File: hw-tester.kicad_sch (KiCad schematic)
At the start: 50 parts, among them J1 AVR-ISP-6, J10 Conn_01x08, J11 Conn_01x08, J12 Conn_01x08, J13 Conn_01x08, J14 BarrelJack, J15 Conn_01x08, J16 Conn_01x08, J17 Conn_01x08, J18 Conn_01x08, J19 USB_B_Mini, J2 Conn_01x08, J3 Conn_01x08, J4 Conn_01x08, J5 Conn_01x08, J6 Conn_01x08, J7 Conn_01x08, J8 Conn_01x08, J9 Conn_01x08, U15 ATmega324PA-M, U28 FT230XQ, U30 ADuM1201AR, X1 IQXO-70

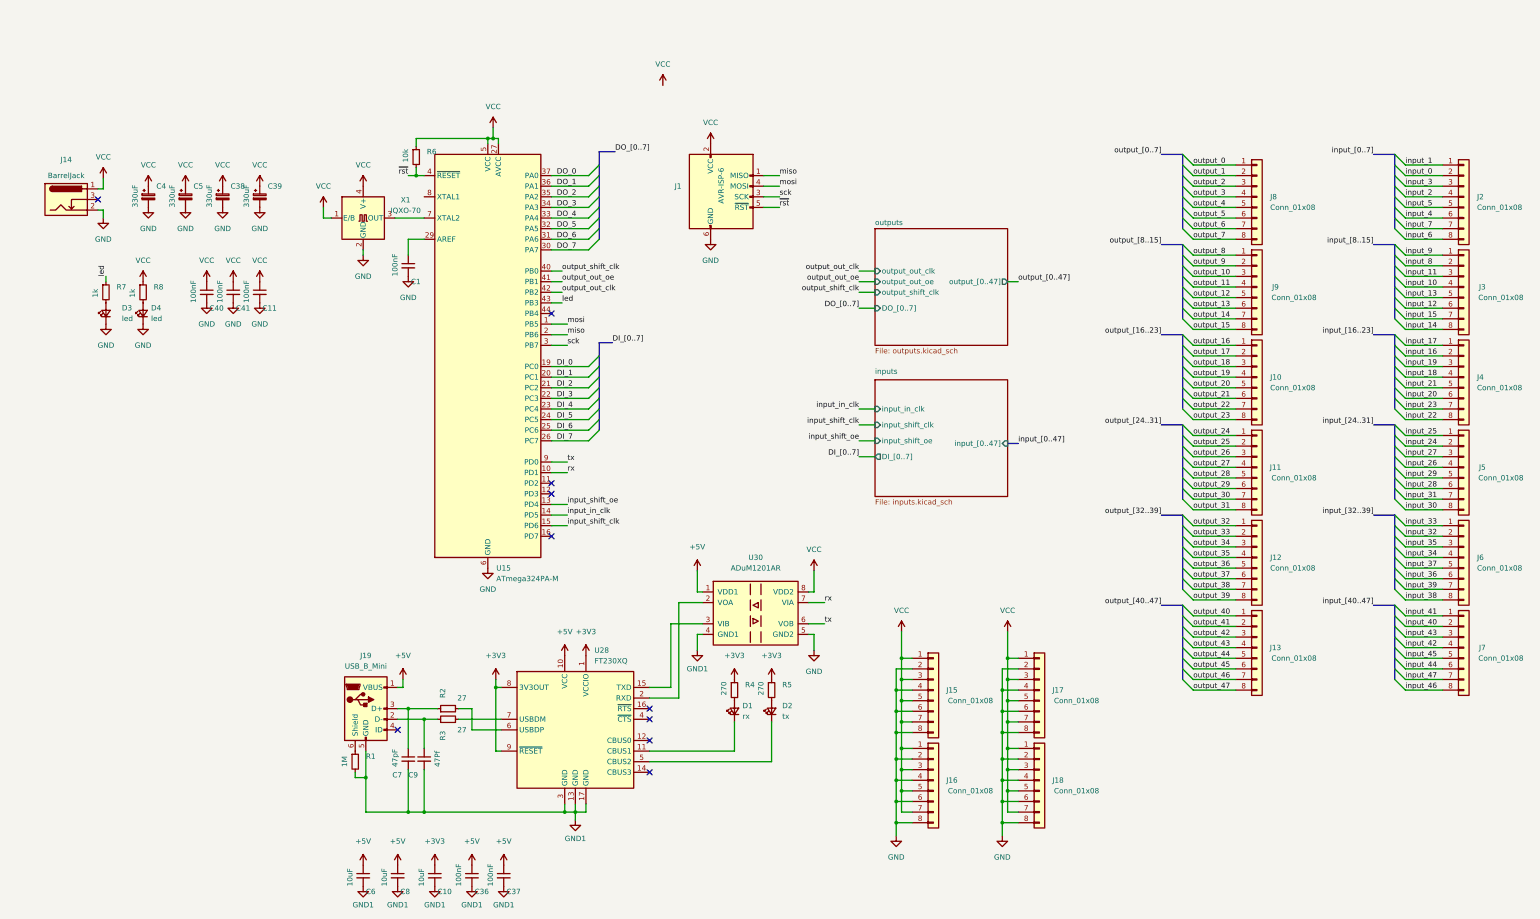
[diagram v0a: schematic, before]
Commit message: Turns out 324As don't really exist anymore
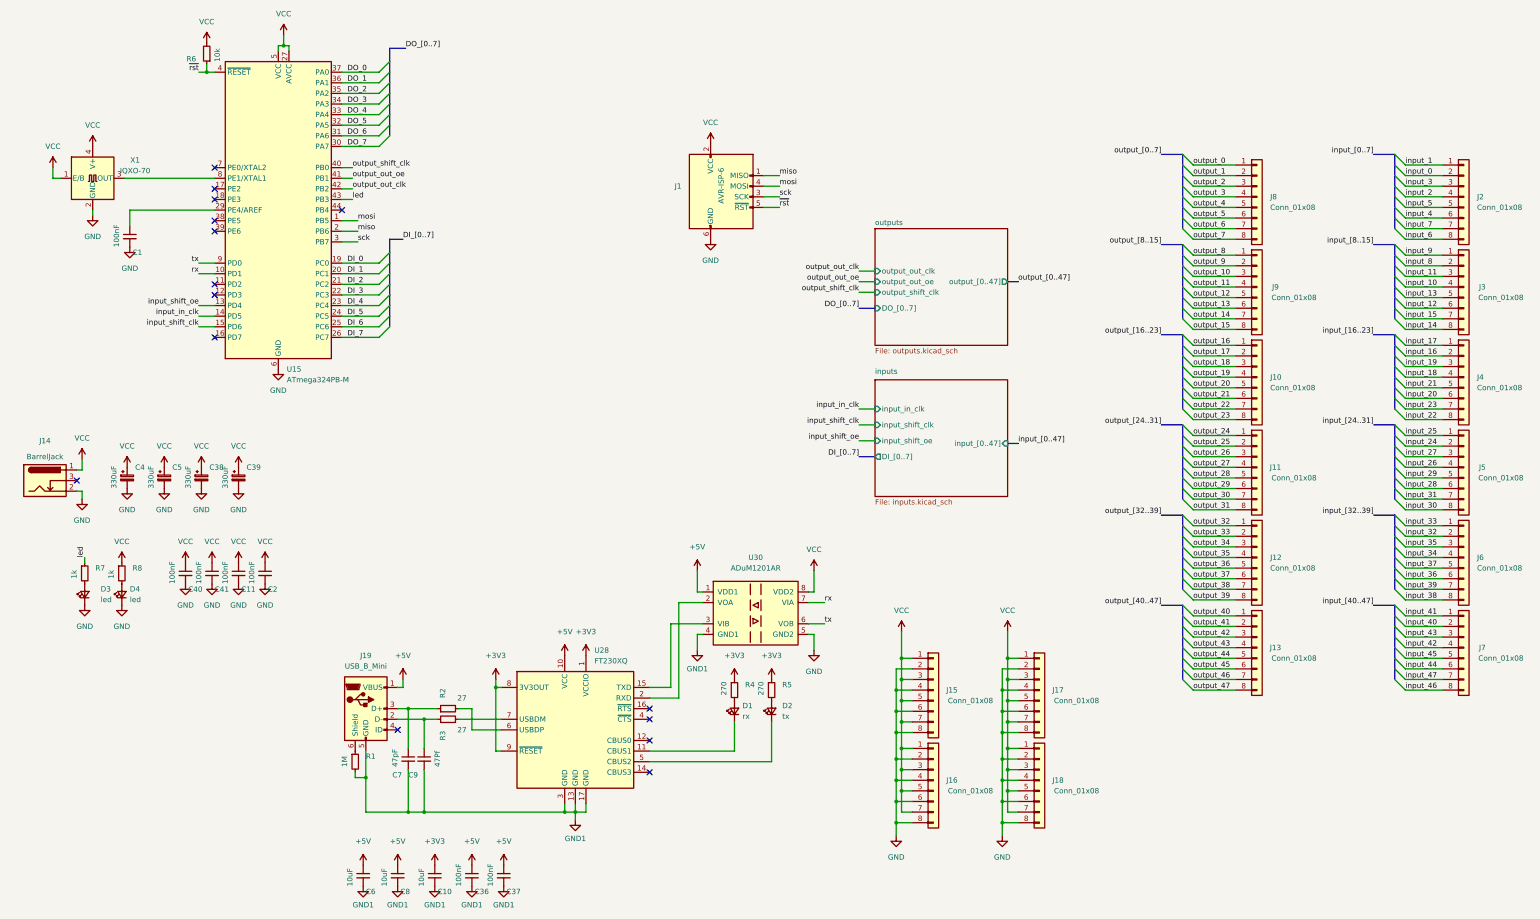
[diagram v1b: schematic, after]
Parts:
- removed U15: ATmega324PA-M, Package_DFN_QFN:QFN-44-1EP_7x7mm_P0.5mm_EP5.2x5.2mm, symbol MCU_Microchip_ATmega:ATmega324PA-M
- added C2: 100nF, Capacitor_SMD:C_0603_1608Metric, symbol Device:C_Small
- added U15: ATmega324PB-M, Package_DFN_QFN:QFN-44-1EP_7x7mm_P0.5mm_EP5.2x5.2mm, symbol MCU_Microchip_ATmega:ATmega324PB-M
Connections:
- net DI_0: now also U15.19 (PC0)
- net DI_1: now also U15.20 (PC1)
- net DI_2: now also U15.21 (PC2)
- net DI_3: now also U15.22 (PC3)
- net DI_4: now also U15.23 (PC4)
- net DI_5: now also U15.24 (PC5)
- net DI_6: now also U15.25 (PC6)
- net DI_7: now also U15.26 (PC7)
- net DO_0: now also U15.37 (PA0)
- net DO_1: now also U15.36 (PA1)
- net DO_2: now also U15.35 (PA2)
- net DO_3: now also U15.34 (PA3)
- net DO_4: now also U15.33 (PA4)
- net DO_5: now also U15.32 (PA5)
- net DO_6: now also U15.31 (PA6)
- net DO_7: now also U15.30 (PA7)
- net GND: now also C2.2, U15.28 (GND), U15.45 (GND), U15.6 (GND)
- net VCC: now also R6.2, C2.1, U15.27 (AVCC), U15.5 (VCC); no longer R6.1
- net input_in_clk: now also U15.14 (PD5)
- net input_shift_clk: now also U15.15 (PD6)
- net input_shift_oe: now also U15.13 (PD4)
- net led: now also U15.43 (PB3)
- net miso: now also U15.2 (PB6)
- net mosi: now also U15.1 (PB5)
- net output_out_clk: now also U15.42 (PB2)
- net output_out_oe: now also U15.41 (PB1)
- net output_shift_clk: now also U15.40 (PB0)
- net rx: now also U15.10 (PD1)
- net sck: now also U15.3 (PB7)
- net tx: now also U15.9 (PD0)
- net ~{rst}: now also R6.1, U15.4 (~{RESET}); no longer R6.2
- net at X1.3 (OUT): now also U15.8 (PE1/XTAL1)
- net at C1.1: now also U15.29 (PE4/AREF)
- no-connect marks 10 -> 15
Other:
- moved on the sheet: C1, C11, C38, C39, C4, C40, C41, C5, D3, D4, J14, R6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

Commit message: firmware
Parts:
- added RN25, RN26: 100K, Resistor_SMD:R_Array_Convex_4x0603, symbol Device:R_Pack04
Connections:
- net GND: now also RN25.6 (R3.2), RN25.7 (R2.2), RN25.8 (R1.2), RN26.1 (R1.1), RN26.2 (R2.1), RN26.4 (R4.1)
- net VCC: now also RN25.5 (R4.2), RN26.3 (R3.1)
- net input_in_clk: now also RN25.3 (R3.1)
- net input_shift_clk: now also RN25.2 (R2.1)
- net input_shift_oe: now also RN25.4 (R4.1)
- net output_out_clk: now also RN26.7 (R2.2)
- net output_out_oe: now also RN26.6 (R3.2)
- net output_shift_clk: now also RN26.5 (R4.2)
- no-connect marks 15 -> 16
